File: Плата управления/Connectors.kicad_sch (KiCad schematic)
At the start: 13 parts, among them J1 A, J11 Conn_01x02_Pin, J12 Conn_01x02_Pin, J13 Conn_01x02_Pin, J14 Conn_01x02_Pin, J15 Conn_01x02_Pin, J2 B, J3 C, J4 Conn_01x02_Pin, J5 Conn_01x03_Pin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

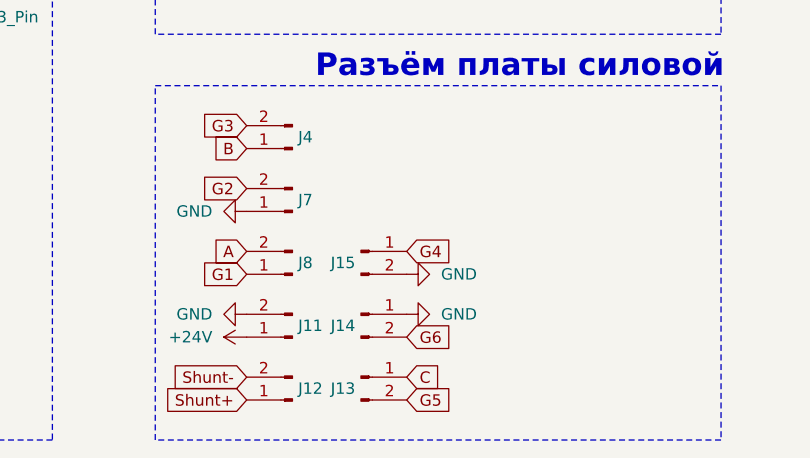
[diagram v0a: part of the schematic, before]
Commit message: Добавил NTC обработку
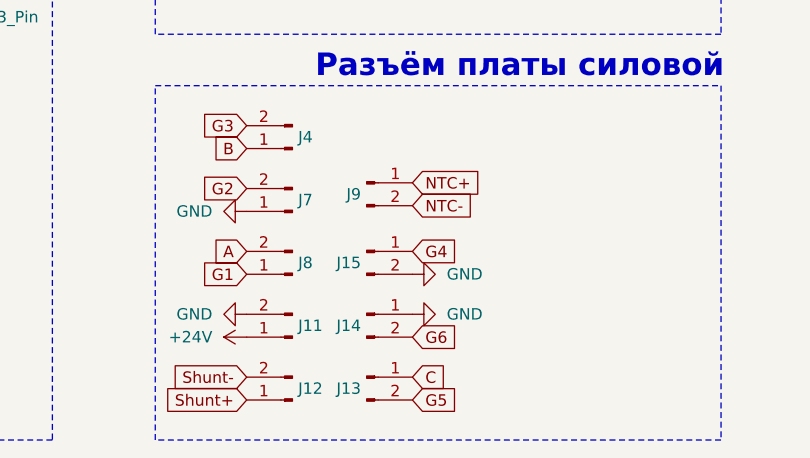
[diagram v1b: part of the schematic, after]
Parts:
- added J9: Conn_01x02_Pin, Connector_PinHeader_2.54mm:PinHeader_1x02_P2.54mm_Vertical, symbol Connector:Conn_01x02_Pin
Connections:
- new net NTC+: J9.1 (Pin_1)
- new net NTC-: J9.2 (Pin_2)
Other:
- moved on the sheet: J13, J14, J15

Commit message: Новые драйвера и разъёмы
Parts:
- removed J11, J12, J13, J14, J15, J4, J7, J8, J9: Conn_01x02_Pin, Connector_PinHeader_2.54mm:PinHeader_1x02_P2.54mm_Vertical, symbol Connector:Conn_01x02_Pin
- added J4, J7: Conn_01x10, Connector_PinHeader_1.27mm:PinHeader_1x10_P1.27mm_Vertical, symbol Connector_Generic:Conn_01x10
- added J9: Conn_01x04, Connector_PinHeader_1.27mm:PinHeader_1x04_P1.27mm_Vertical, symbol Connector_Generic:Conn_01x04
- J1, J2, J3: footprint Connector_My:Power_Wire -> Connector_My:Hole_9mm
- Jd1: renamed from J6; footprint Connector_PinHeader_2.00mm:PinHeader_2x04_P2.00mm_Vertical -> Connector_PinHeader_1.27mm:PinHeader_2x04_P1.27mm_Vertical
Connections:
- net +24V: now also J9.3 (Pin_3)
- net A: now also J4.10 (Pin_10)
- net B: now also J4.4 (Pin_4)
- net C: now also J7.10 (Pin_10)
- net CAN1H: now also J5.3 (Pin_3); no longer J5.2 (Pin_2)
- net CAN1L: now also J5.2 (Pin_2); no longer J5.3 (Pin_3)
- net G1: now also J4.9 (Pin_9)
- net G2: now also J4.5 (Pin_5)
- net G3: now also J4.3 (Pin_3)
- net G4: now also J7.3 (Pin_3)
- net G5: now also J7.9 (Pin_9)
- net G6: now also J7.5 (Pin_5)
- net GND: now also J4.6 (Pin_6), J7.4 (Pin_4), J7.6 (Pin_6), J9.4 (Pin_4)
- net Shunt+: now also J9.2 (Pin_2)
- net Shunt-: now also J9.1 (Pin_1)
- new net NTC_A+: J4.7 (Pin_7)
- new net NTC_A-: J4.8 (Pin_8)
- new net NTC_B+: J4.2 (Pin_2)
- new net NTC_B-: J4.1 (Pin_1)
- new net NTC_C+: J7.7 (Pin_7)
- new net NTC_C-: J7.8 (Pin_8)
- no-connect marks 0 -> 3

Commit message: Добавил разъёмф для крепления
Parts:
- added J6, J8: Conn_01x02, Connector_PinHeader_1.27mm:PinHeader_1x02_P1.27mm_Vertical, symbol Connector_Generic:Conn_01x02
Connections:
- no-connect marks 3 -> 7
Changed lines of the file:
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@@
+	)
+	(no_connect
+		(at 91.44 110.49)
 	)
 	(no_connect
@@
 	)
 	(no_connect
+		(at 91.44 120.65)
+	)
+	(no_connect
 		(at 45.085 89.535)
+	)
+	(no_connect
+		(at 91.44 118.11)
+	)
+	(no_connect
+		(at 91.44 113.03)
 	)
 	(rectangle
@@
 	)
 	(symbol
+		(lib_id "Connector_Generic:Conn_01x02")
+		(at 96.52 110.49 0)
+		(unit 1)
+		(exclude_from_sim no)
+		(in_bom yes)
+		(on_board yes)
+		(dnp no)
+		(fields_autoplaced yes)
+		(property "Reference" "J6"
+			(at 99.06 110.4899 0)
+			(effects
+				(font
+					(size 1.27 1.27)
+				)
+				(justify left)
+			)
+		)
+		(property "Value" "Conn_01x02"
+			(at 99.06 113.0299 0)
+			(effects
+				(font
+					(size 1.27 1.27)
+				)
+				(justify left)
+				(hide yes)
+			)
+		)
+		(property "Footprint" "Connector_PinHeader_1.27mm:PinHeader_1x02_P1.27mm_Vertical"
+			(at 96.52 110.49 0)
+			(effects
+				(font
+					(size 1.27 1.27)
+				)
+				(hide yes)
+			)
+		)
+		(property "Datasheet" "~"
+			(at 96.52 110.49 0)
+			(effects
+				(font
+					(size 1.27 1.27)
+				)
+				(hide yes)
+			)
+		)
+		(property "Description" "Generic connector, single row, 01x02, script generated (kicad-library-utils/schlib/autogen/connector/)"
+			(at 96.52 110.49 0)
+			(effects
+				(font
+					(size 1.27 1.27)
+				)
+				(hide yes)
+			)
+		)
+		(pin "1"
+		)
+		(pin "2"
+		)
+		(instances
+			(project ""
+				(path "/75f4c67c-bbde-4446-8f82-67797a1b269f/f5e732cc-be4b-4207-bf28-0691ff32221d"
+					(reference "J6")
+					(unit 1)
+				)
+			)
+		)
+	)
+	(symbol
 		(lib_id "power:GND")
 		(at 160.02 123.19 270)
@@
 					(unit 1)
 				)
+			)
+		)
+	)
+	(symbol
+		(lib_id "Connector_Generic:Conn_01x02")
+		(at 96.52 118.11 0)
+		(unit 1)
+		(exclude_from_sim no)
+		(in_bom yes)
+		(on_board yes)
+		(dnp no)
+		(fields_autoplaced yes)
+		(property "Reference" "J8"
+			(at 99.06 118.1099 0)
+			(effects
+				(font
+					(size 1.27 1.27)
+				)
+				(justify left)
+			)
+		)
+		(property "Value" "Conn_01x02"
+			(at 99.06 120.6499 0)
+			(effects
+				(font
+					(size 1.27 1.27)
+				)
+				(justify left)
+				(hide yes)
+			)
+		)
+		(property "Footprint" "Connector_PinHeader_1.27mm:PinHeader_1x02_P1.27mm_Vertical"
+			(at 96.52 118.11 0)
+			(effects
+				(font
+					(size 1.27 1.27)
+				)
+				(hide yes)
+			)
+		)
+		(property "Datasheet" "~"
+			(at 96.52 118.11 0)
+			(effects
+				(font
+					(size 1.27 1.27)
+				)
+				(hide yes)
+			)
+		)
+		(property "Description" "Generic connector, single row, 01x02, script generated (kicad-library-utils/schlib/autogen/connector/)"
+			(at 96.52 118.11 0)
+			(effects
+				(font
+					(size 1.27 1.27)
+				)
+				(hide yes)
+			)
+		)
+		(pin "1"
+		)
+		(pin "2"
+		)
+		(instances
+			(project "Плата управления"
+				(path "/75f4c67c-bbde-4446-8f82-67797a1b269f/f5e732cc-be4b-4207-bf28-0691ff32221d"
+					(reference "J8")
+					(unit 1)
+				)

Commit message: Добавил модель плты
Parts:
- removed J5: Conn_01x03_Pin, Connector_PinHeader_2.54mm:PinHeader_1x03_P2.54mm_Vertical, symbol Connector:Conn_01x03_Pin
- added J11, J12, J13, J14, J15, J5: C, Connector_My:Wire_one, symbol Connector_Generic:Conn_01x01
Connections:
- net CAN1H: now also J13.1 (Pin_1), J5.1 (Pin_1)
- net CAN1L: now also J11.1 (Pin_1), J14.1 (Pin_1)
- net GND: now also J12.1 (Pin_1), J15.1 (Pin_1)

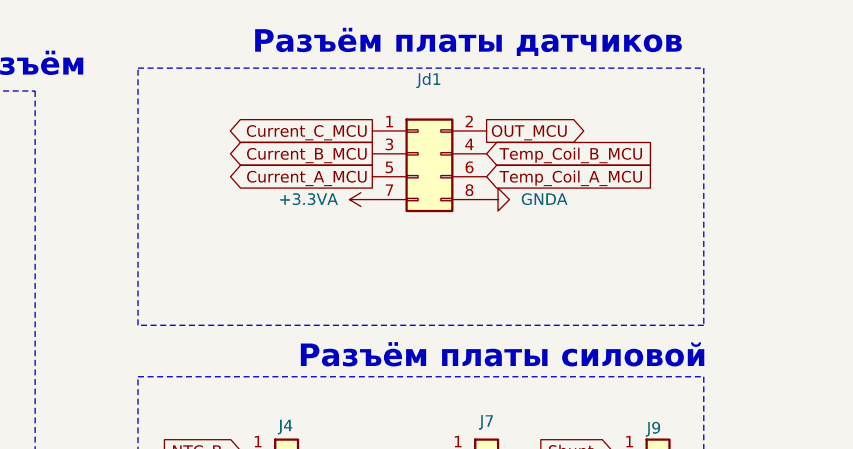
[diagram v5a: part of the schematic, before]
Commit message: Добавил съемные разъемы
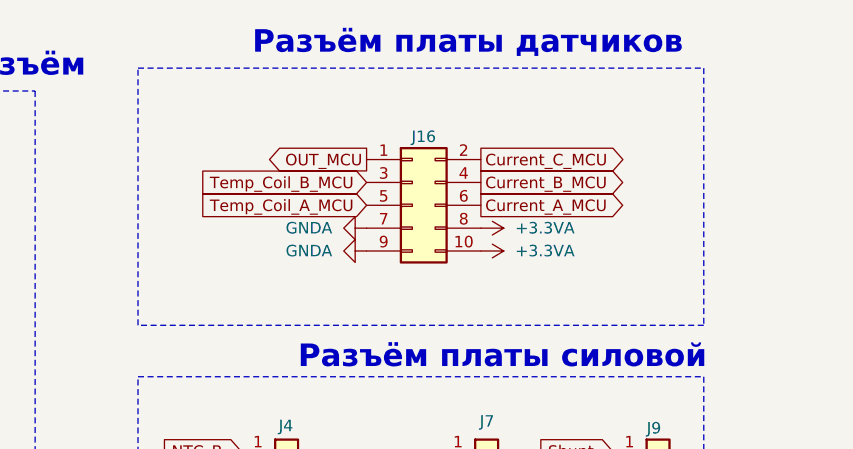
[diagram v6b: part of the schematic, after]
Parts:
- removed Jd1: Conn_02x04_Odd_Even, Connector_PinHeader_1.27mm:PinHeader_2x04_P1.27mm_Vertical, symbol Connector_Generic:Conn_02x04_Odd_Even
- added J16: Conn_02x05_Odd_Even, Connector_PinSocket_1.27mm:PinSocket_2x05_P1.27mm_Vertical, symbol Connector_Generic:Conn_02x05_Odd_Even
- J6, J8: footprint Connector_PinHeader_1.27mm:PinHeader_1x02_P1.27mm_Vertical -> Connector_PinSocket_1.27mm:PinSocket_1x02_P1.27mm_Vertical
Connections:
- net +3.3VA: now also J16.10 (Pin_10), J16.8 (Pin_8)
- net Current_A_MCU: now also J16.6 (Pin_6)
- net Current_B_MCU: now also J16.4 (Pin_4)
- net Current_C_MCU: now also J16.2 (Pin_2)
- net GNDA: now also J16.7 (Pin_7), J16.9 (Pin_9)
- net OUT_MCU: now also J16.1 (Pin_1)
- net Temp_Coil_A_MCU: now also J16.5 (Pin_5)
- net Temp_Coil_B_MCU: now also J16.3 (Pin_3)

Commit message: Изменения: добавил папку с отчетностью
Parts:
- J16: footprint Connector_PinSocket_1.27mm:PinSocket_2x05_P1.27mm_Vertical -> Connector_PinHeader_1.27mm:PinHeader_2x05_P1.27mm_Vertical
- J6, J8: footprint Connector_PinSocket_1.27mm:PinSocket_1x02_P1.27mm_Vertical -> Connector_PinHeader_1.27mm:PinHeader_1x02_P1.27mm_Vertical
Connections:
- net +3.3VA: now also J16.7 (Pin_7), J16.9 (Pin_9); no longer J16.10 (Pin_10), J16.8 (Pin_8)
- net Current_A_MCU: now also J16.5 (Pin_5); no longer J16.6 (Pin_6)
- net Current_B_MCU: now also J16.3 (Pin_3); no longer J16.4 (Pin_4)
- net Current_C_MCU: now also J16.1 (Pin_1); no longer J16.2 (Pin_2)
- net GNDA: now also J16.10 (Pin_10), J16.8 (Pin_8); no longer J16.7 (Pin_7), J16.9 (Pin_9)
- net OUT_MCU: now also J16.2 (Pin_2); no longer J16.1 (Pin_1)
- net Temp_Coil_A_MCU: now also J16.6 (Pin_6); no longer J16.5 (Pin_5)
- net Temp_Coil_B_MCU: now also J16.4 (Pin_4); no longer J16.3 (Pin_3)
- no-connect marks 7 -> 9
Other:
- moved on the sheet: J1, J11, J12, J13, J14, J15, J16, J2, J3, J4, J5, J6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
